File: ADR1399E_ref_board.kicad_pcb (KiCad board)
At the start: 4 copper layers, 119 x 60 mm, 106 parts, among them J1 Conn_01x02_Pin, J2 USB_C_Receptacle_PowerOnly_6P, J3 Conn_Coaxial, J4 S4B-XH-A, P1 JST_B2P_VH, Q1 MMBT3906, U1 LT3042xMSE, U2 TPS61085DGK, U3 OPA182IDR, U4 OPA994IDR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

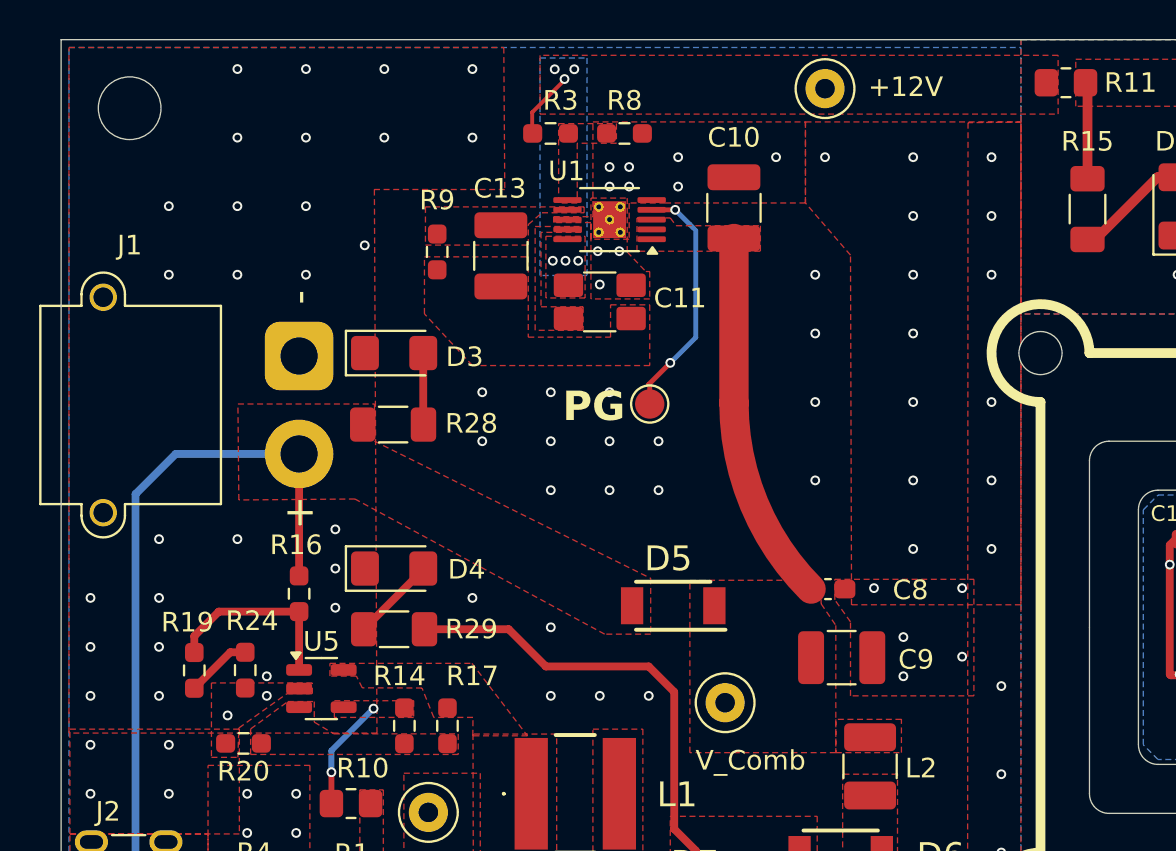
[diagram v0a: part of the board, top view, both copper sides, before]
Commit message: updated PCB to adp7118/42
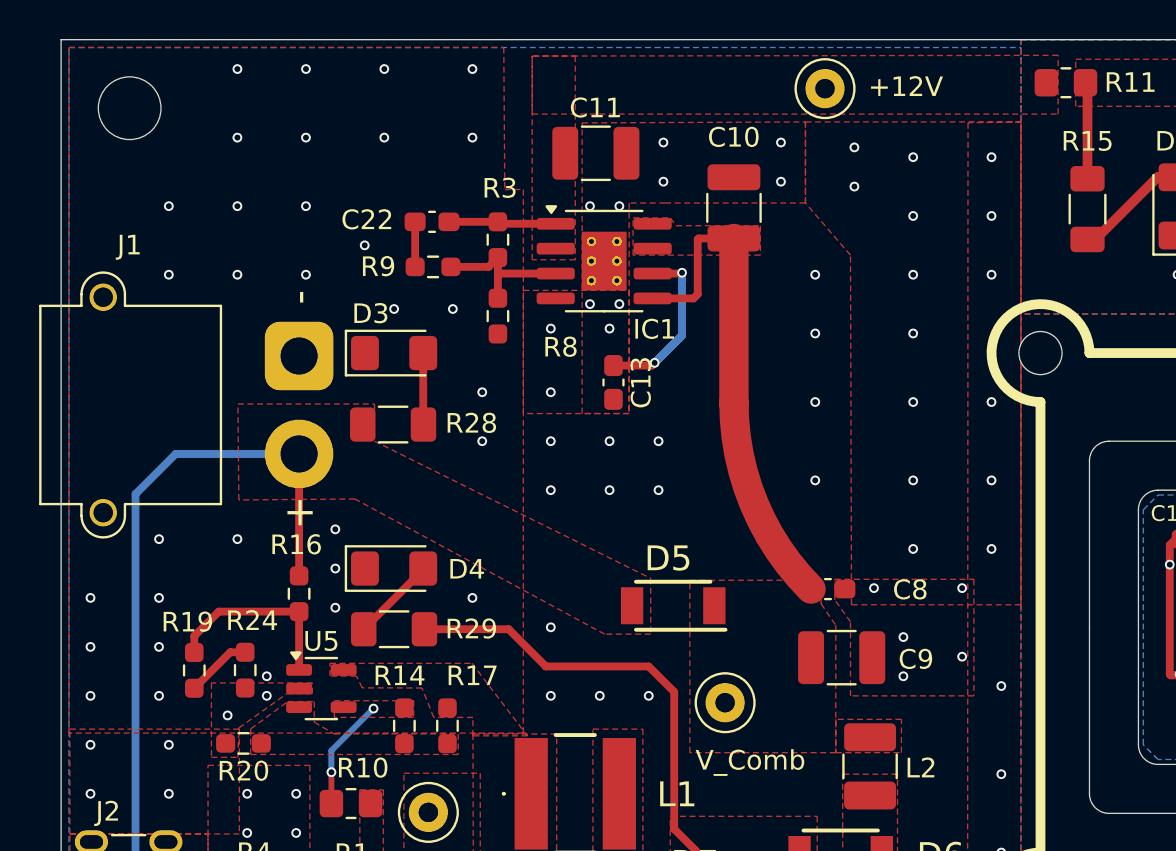
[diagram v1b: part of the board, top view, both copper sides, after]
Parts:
- removed TP5: TestPoint, TestPoint:TestPoint_Pad_D1.5mm
- removed U1: LT3042xMSE, Package_SO:MSOP-10-1EP_3x3mm_P0.5mm_EP1.68x1.88mm_ThermalVias
- added C22: 1uF 25V, Capacitor_SMD:C_0603_1608Metric_Pad1.08x0.95mm_HandSolder, F.Cu at (49.9, 83.3)
- added IC1: ADP7118ARDZ-R7, Package_SO:SOIC-8-1EP_3.9x4.9mm_P1.27mm_EP2.29x3mm_ThermalVias, F.Cu at (58.7, 85.3)
- C11: footprint nightmechanic_pcb:3225_Kelvin_4port -> Capacitor_SMD:C_1210_3225Metric_Pad1.33x2.70mm_HandSolder
- C13: value 10uF 50V -> 3n 25V; footprint Capacitor_SMD:C_1210_3225Metric_Pad1.33x2.70mm_HandSolder -> Capacitor_SMD:C_0603_1608Metric_Pad1.08x0.95mm_HandSolder
- R8: value 5.1k -> 20k 0.1%
- R9: value 120k 0.1% -> 10k 0.5% 25ppm
- moved R8 11.3 mm to (53.3, 88.1), turned to -90 degrees
- moved C13 8.65 mm to (59.2, 91.5)
- moved C11 7.59 mm to (58.3, 79.8)
- moved R3 6.05 mm to (53.3, 84.2), turned to -90 degrees
- moved R9 0.79 mm to (50.0, 85.6), turned to 0 degrees
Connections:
- C11 pad 1: Net-(C11-Pad1) -> +12V
- C13 pad 1: Net-(U1-SET) -> Net-(IC1-SS)
- C13 pad 2: Net-(C11-Pad1) -> GND
- J1 pad : GND -> (no net)
- R3 pad 2: Net-(U1-PGFB) -> Net-(IC1-SENSE/ADJ)
- R8 pad 1: Net-(U1-PGFB) -> Net-(IC1-SENSE/ADJ)
- R9 pad 1: Net-(U1-SET) -> Net-(C22-Pad2)
- R9 pad 2: Net-(C11-Pad1) -> Net-(IC1-SENSE/ADJ)
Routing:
- net Net-(U1-PG): track 12.4 -> 0.00 mm, vias 2 -> 0
- net Net-(IC1-SS): track 0.00 -> 10.7 mm, vias 0 -> 2
- net Net-(IC1-SENSE/ADJ): track 0.00 -> 7.64 mm
- net /Inductance: track 18.9 -> 25.9 mm
- net +12V: track 0.00 -> 5.49 mm, vias 6 -> 0
- net Net-(C22-Pad2): track 0.00 -> 2.30 mm
- net GND: vias 311 -> 313
- removed copper zone on B.Cu, net +12V
- removed copper zone on F.Cu, net Net-(C11-Pad1)
- removed copper zone on F.Cu, net Net-(U1-OUTS)
- removed copper zone on F.Cu, net Net-(U1-PGFB)
- removed copper zone on F.Cu, net Net-(U1-SET)
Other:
- board text removed: "PG"

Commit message: changed to 15V, adp7142
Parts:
- IC1: value ADP7118ARDZ-R7 -> ADP7142ARDZ-R7
- R6: value 17.8k 0.1% -> 14.7k 0.1%
- R8: value 20k 0.1% -> 15.8k 0.1%
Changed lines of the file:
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@@
 			)
 		)
-		(property "Value" "17.8k 0.1%"
+		(property "Value" "14.7k 0.1%"
 			(at 0 1.43 90)
 			(layer "F.Fab")
@@
 			)
 		)
-		(property "Value" "20k 0.1%"
+		(property "Value" "15.8k 0.1%"
 			(at 0 1.43 90)
 			(layer "F.Fab")
@@
 			)
 		)
-		(property "Value" "ADP7118ARDZ-R7"
+		(property "Value" "ADP7142ARDZ-R7"
 			(at 0 3.4 0)
 			(layer "F.Fab")
@@
 			)
 		)
-		(property "Manufacturer_Part_Number" "ADP7118ARDZ-R7"
+		(property "Manufacturer_Part_Number" "ADP7142ARDZ-R7"
 			(at 0 0 0)
 			(unlocked yes)

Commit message: cleanup
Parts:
- R24: value 180k 0.1% -> 120k 0.1%
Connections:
- net +12V renamed +15V
- net /12V_Out renamed /15V_Out
- J1 pad : (no net) -> GND
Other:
- board text added: "+15V"
- board text removed: "+12V"
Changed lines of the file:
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@@
 	(net 31 "Net-(U2-EN)")
 	(net 32 "Net-(U2-FB)")
-	(net 33 "+12V")
+	(net 33 "+15V")
 	(net 34 "Net-(IC1-SENSE{slash}ADJ)")
 	(net 35 "Net-(U2-COMP)")
@@
 	(net 47 "Net-(D6-K)")
 	(net 48 "Net-(D7-A)")
-	(net 49 "/12V_Out")
+	(net 49 "/15V_Out")
 	(net 50 "/LMT_VCC")
 	(net 51 "/LMT_OUT")
@@
 		(tags "SOT TO_SOT_SMD")
 		(property "Reference" "Q1"
-			(at 0 -2.4 0)
+			(at 0 -2.6 0)
 			(layer "F.SilkS")
 			(effects
@@
 			(layers "F.Cu" "F.Mask" "F.Paste")
 			(roundrect_rratio 0.25)
-			(net 49 "/12V_Out")
+			(net 49 "/15V_Out")
 			(pintype "passive")
 		)
@@
 			(layers "*.Cu" "*.Mask")
 			(remove_unused_layers no)
-			(net 33 "+12V")
+			(net 33 "+15V")
 			(pinfunction "1")
 			(pintype "passive")
@@
 			(layers "F.Cu" "F.Mask" "F.Paste")
 			(roundrect_rratio 0.25)
-			(net 49 "/12V_Out")
+			(net 49 "/15V_Out")
 			(pintype "passive")
 		)
@@
 			(layers "F.Cu" "F.Mask" "F.Paste")
 			(roundrect_rratio 0.208333)
-			(net 49 "/12V_Out")
+			(net 49 "/15V_Out")
 			(pintype "passive")
 		)
@@
 			(layers "F.Cu" "F.Mask" "F.Paste")
 			(roundrect_rratio 0.208333)
-			(net 33 "+12V")
+			(net 33 "+15V")
 			(pintype "passive")
 		)
@@
 			(layers "F.Cu" "F.Mask" "F.Paste")
 			(roundrect_rratio 0.208333)
-			(net 49 "/12V_Out")
+			(net 49 "/15V_Out")
 			(pintype "passive")
 		)
@@
 		(tags "resistor handsolder")
 		(property "Reference" "R8"
-			(at 1.6 -3.2 180)
+			(at -0.8125 1.8 180)
 			(layer "F.SilkS")
 			(effects
@@
 			(layers "F.Cu" "F.Mask" "F.Paste")
 			(roundrect_rratio 0.25)
-			(net 49 "/12V_Out")
+			(net 49 "/15V_Out")
 			(pintype "passive")
 		)
@@
 			(layers "F.Cu" "F.Mask" "F.Paste")
 			(roundrect_rratio 0.192308)
-			(net 49 "/12V_Out")
+			(net 49 "/15V_Out")
 			(pintype "passive")
 		)
@@
 			(layers "F.Cu" "F.Mask" "F.Paste")
 			(roundrect_rratio 0.25)
-			(net 49 "/12V_Out")
+			(net 49 "/15V_Out")
 			(pintype "passive")
 		)
@@
 			(layers "F.Cu" "F.Mask" "F.Paste")
 			(roundrect_rratio 0.188679)
-			(net 33 "+12V")
+			(net 33 "+15V")
 			(pintype "passive")
 		)
@@
 			(layers "F.Cu" "F.Mask" "F.Paste")
 			(roundrect_rratio 0.25)
-			(net 33 "+12V")
+			(net 33 "+15V")
 			(pinfunction "VOUT_1")
 			(pintype "power_out")
@@
 			(layers "F.Cu" "F.Mask" "F.Paste")
 			(roundrect_rratio 0.25)
-			(net 33 "+12V")
+			(net 33 "+15V")
 			(pinfunction "VOUT_2")
 			(pintype "passive")
@@
 			(layers "F.Cu" "F.Mask" "F.Paste")
 			(roundrect_rratio 0.25)
-			(net 49 "/12V_Out")
+			(net 49 "/15V_Out")
 			(pinfunction "HEATER+")
 			(pintype "power_in")
@@
 			(layers "F.Cu" "F.Mask" "F.Paste")
 			(roundrect_rratio 0.25)
-			(net 49 "/12V_Out")
+			(net 49 "/15V_Out")
 			(pintype "passive")
 		)
@@
 		(tags "capacitor handsolder")
 		(property "Reference" "C13"
-			(at 0 -1.43 90)
+			(at 0.9 -2.3 180)
 			(layer "F.SilkS")
 			(effects
@@
 			(size 2.169158 0.582132)
 			(layers "F.Cu" "F.Mask" "F.Paste")
-			(net 49 "/12V_Out")
+			(net 49 "/15V_Out")
 			(pinfunction "V+")
 			(pintype "power_in")
@@
 			(layers "*.Cu" "*.Mask")
 			(remove_unused_layers no)
+			(net 1 "GND")
 		)
 		(pad "" thru_hole circle
@@
 			(layers "*.Cu" "*.Mask")
 			(remove_unused_layers no)
+			(net 1 "GND")
 		)
 		(pad "1" thru_hole roundrect
@@
 			)
 		)
-		(property "Value" "180k 0.1%"
+		(property "Value" "120k 0.1%"
 			(at 0 1.43 90)
 			(layer "F.Fab")
@@
 			(layers "F.Cu" "F.Mask" "F.Paste")
 			(roundrect_rratio 0.25)
-			(net 33 "+12V")
+			(net 33 "+15V")
 			(pintype "passive")
 		)
@@
 			(layers "F.Cu" "F.Mask" "F.Paste")
 			(roundrect_rratio 0.25)
-			(net 33 "+12V")
+			(net 33 "+15V")
 			(pintype "passive")
 		)
@@
 	)
 	(gr_text "V_REF"
-		(at 107.2 92.4 0)
+		(at 108.3 92.4 0)
 		(layer "F.SilkS")
 		(effects
@@
 		)
 	)
-	(gr_text "+12V"
+	(gr_text "+15V"
 		(at 72.2 77 0)
 		(layer "F.SilkS")
@@
 	(zone
 		(net 33)
-		(net_name "+12V")
+		(net_name "+15V")
 		(layer "F.Cu")
 		(hatch edge 0.5)
@@
 	(zone
 		(net 49)
-		(net_name "/12V_Out")
+		(net_name "/15V_Out")
 		(layer "F.Cu")
 		(hatch edge 0.5)
@@
 	(zone
 		(net 49)
-		(net_name "/12V_Out")
+		(net_name "/15V_Out")
 		(layer "F.Cu")
 		(hatch edge 0.5)
@@
 	(zone
 		(net 49)
-		(net_name "/12V_Out")
+		(net_name "/15V_Out")
 		(layer "F.Cu")
 		(hatch edge 0.5)
@@
 	(zone
 		(net 33)
-		(net_name "+12V")
+		(net_name "+15V")
 		(layer "F.Cu")
 		(hatch edge 0.5)

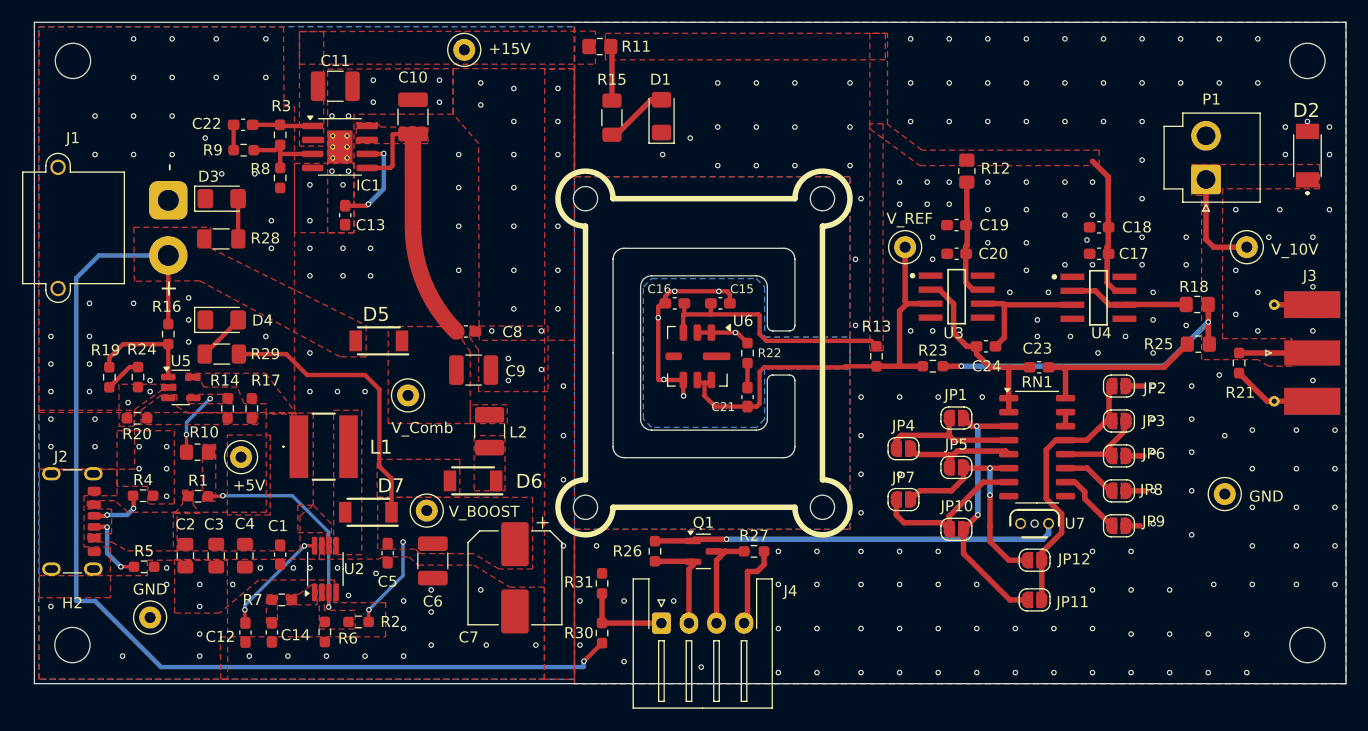
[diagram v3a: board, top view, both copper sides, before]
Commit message: Replaced Boost enable comparator with N-MOS
also changed Vbatt divider resistor value
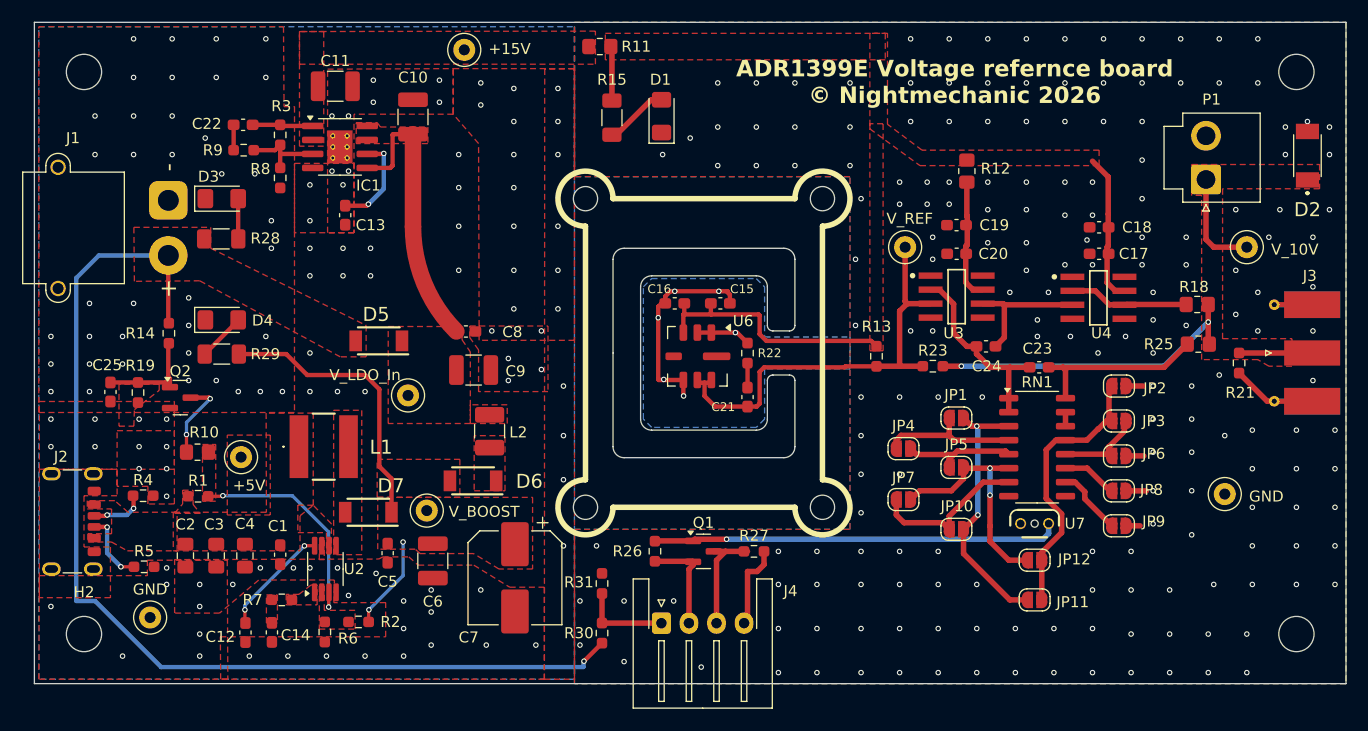
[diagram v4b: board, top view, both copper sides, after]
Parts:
- removed R16, R17, R20: 1Meg, Resistor_SMD:R_0603_1608Metric_Pad0.98x0.95mm_HandSolder
- removed R24: 120k 0.1%, Resistor_SMD:R_0603_1608Metric_Pad0.98x0.95mm_HandSolder
- removed U5: TL331, Package_TO_SOT_SMD:SOT-23-5
- added C25: 100nF 50V, Capacitor_SMD:C_0603_1608Metric_Pad1.08x0.95mm_HandSolder, F.Cu at (37.9, 107.5)
- added Q2: 2N7002, Package_TO_SOT_SMD:SOT-23, F.Cu at (44.2, 108.0)
- R14: value 1Meg -> 180k 0.1%
- R31: value 17.8k 0.1% -> 15.8k 0.1%
- moved R14 8.65 mm to (43.2, 102.2), turned to -90 degrees
- moved R19 2.95 mm to (40.4, 107.6)
- moved H2 1.45 mm to (35.5, 129.5)
- moved H1 1.41 mm to (35.5, 78.5)
- moved H3 1.41 mm to (145.5, 78.5)
- moved H4 1.41 mm to (145.5, 129.5)
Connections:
- R14 pad 1: Net-(U5-+) -> +BATT
- R14 pad 2: /Boost_En -> Net-(Q2-G)
- R19 pad 1: Net-(U5--) -> Net-(Q2-G)
- R19 pad 2: Net-(R19-Pad2) -> GND
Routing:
- net Net-(U5--): track 9.68 -> 0.00 mm
- net Net-(Q2-G): track 0.00 -> 9.54 mm
- net Net-(R19-Pad2): track 3.36 -> 0.00 mm
- net /Boost_En: track 5.74 -> 7.56 mm
- net GND: vias 313 -> 319
- removed copper zone on F.Cu, net /Boost_En
- removed copper zone on F.Cu, net Net-(U5-+)
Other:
- board text added: "ADR1399E Voltage refernce board © Nightmechanic 2026"
